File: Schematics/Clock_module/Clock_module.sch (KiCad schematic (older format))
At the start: 38 parts, among them J1 Conn_01x06_Female, J2 Power Input, SW1 Mode, SW2 Step, U1 NE555, U2 NE555, U3 NE555, U4 74LS04, U5 74LS32, U6 74LS08

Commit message: Redesign in progress
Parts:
- J2: symbol Connector:Barrel_Jack_MountingPin -> Connector:Barrel_Jack
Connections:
- no-connect marks 2 -> 1
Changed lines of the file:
@@
 	7900 5150 7900 5050
 $Comp
-L Connector:Barrel_Jack_MountingPin J2
+L Connector:Barrel_Jack J2
 U 1 1 5E4C3442
 P 2700 1400
@@
 	1    0    0    -1
 $EndComp
-NoConn ~ 2700 1700
 Wire Wire Line
 	3000 1300 3000 1250

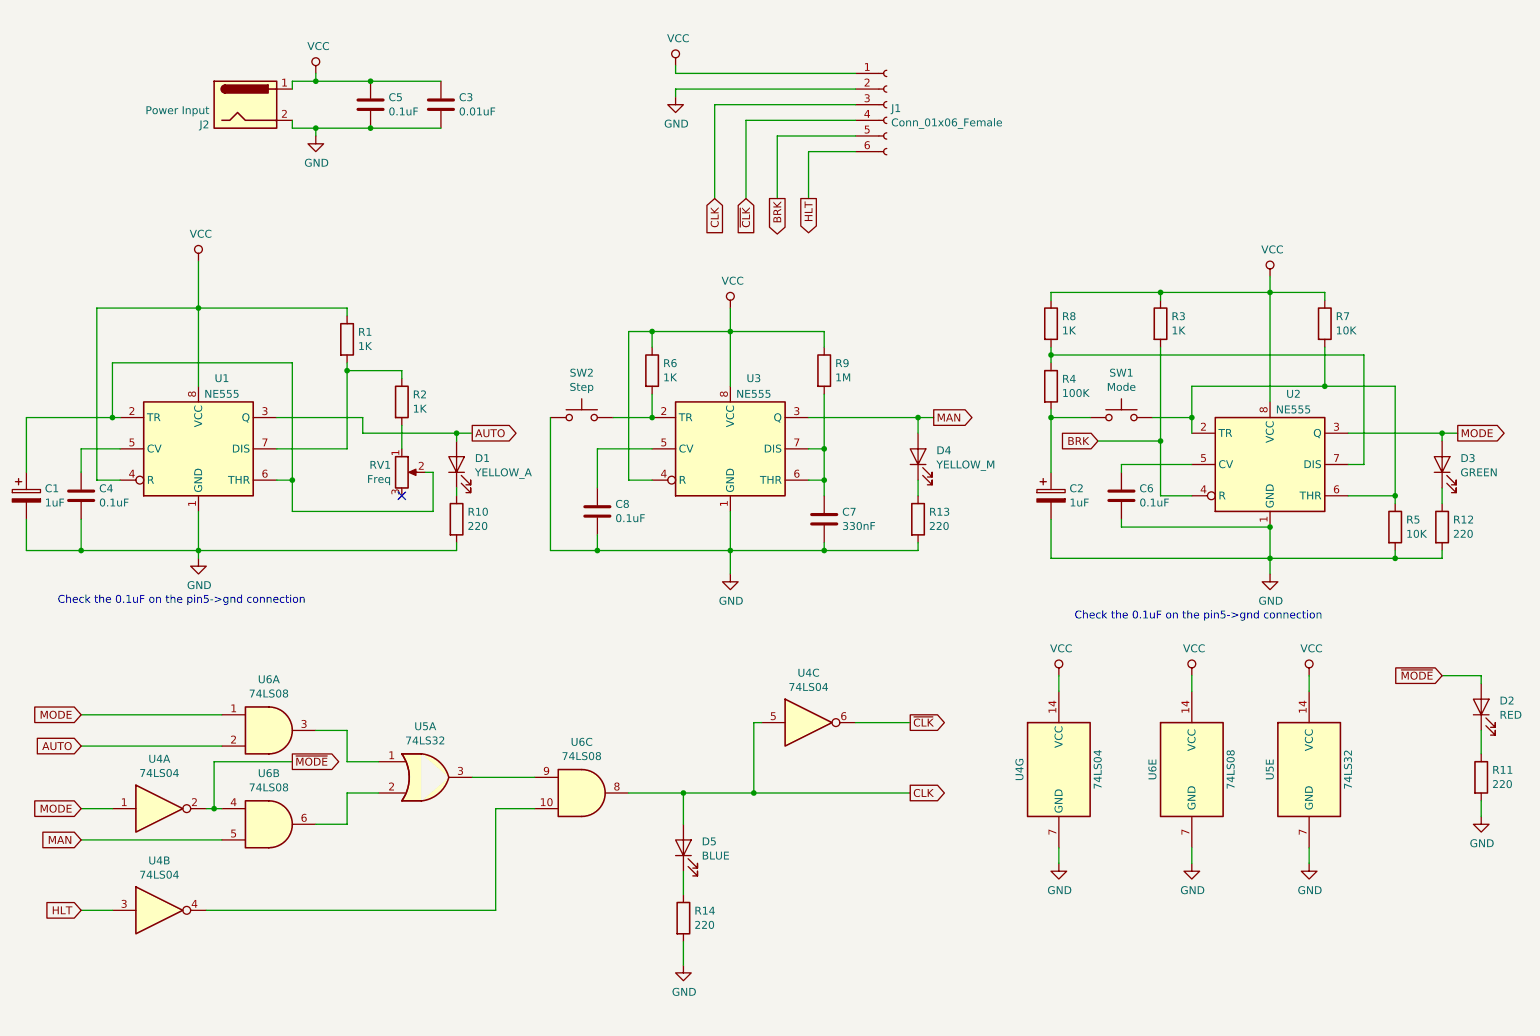
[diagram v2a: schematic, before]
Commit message: Added missing pull-down resistor to clock module
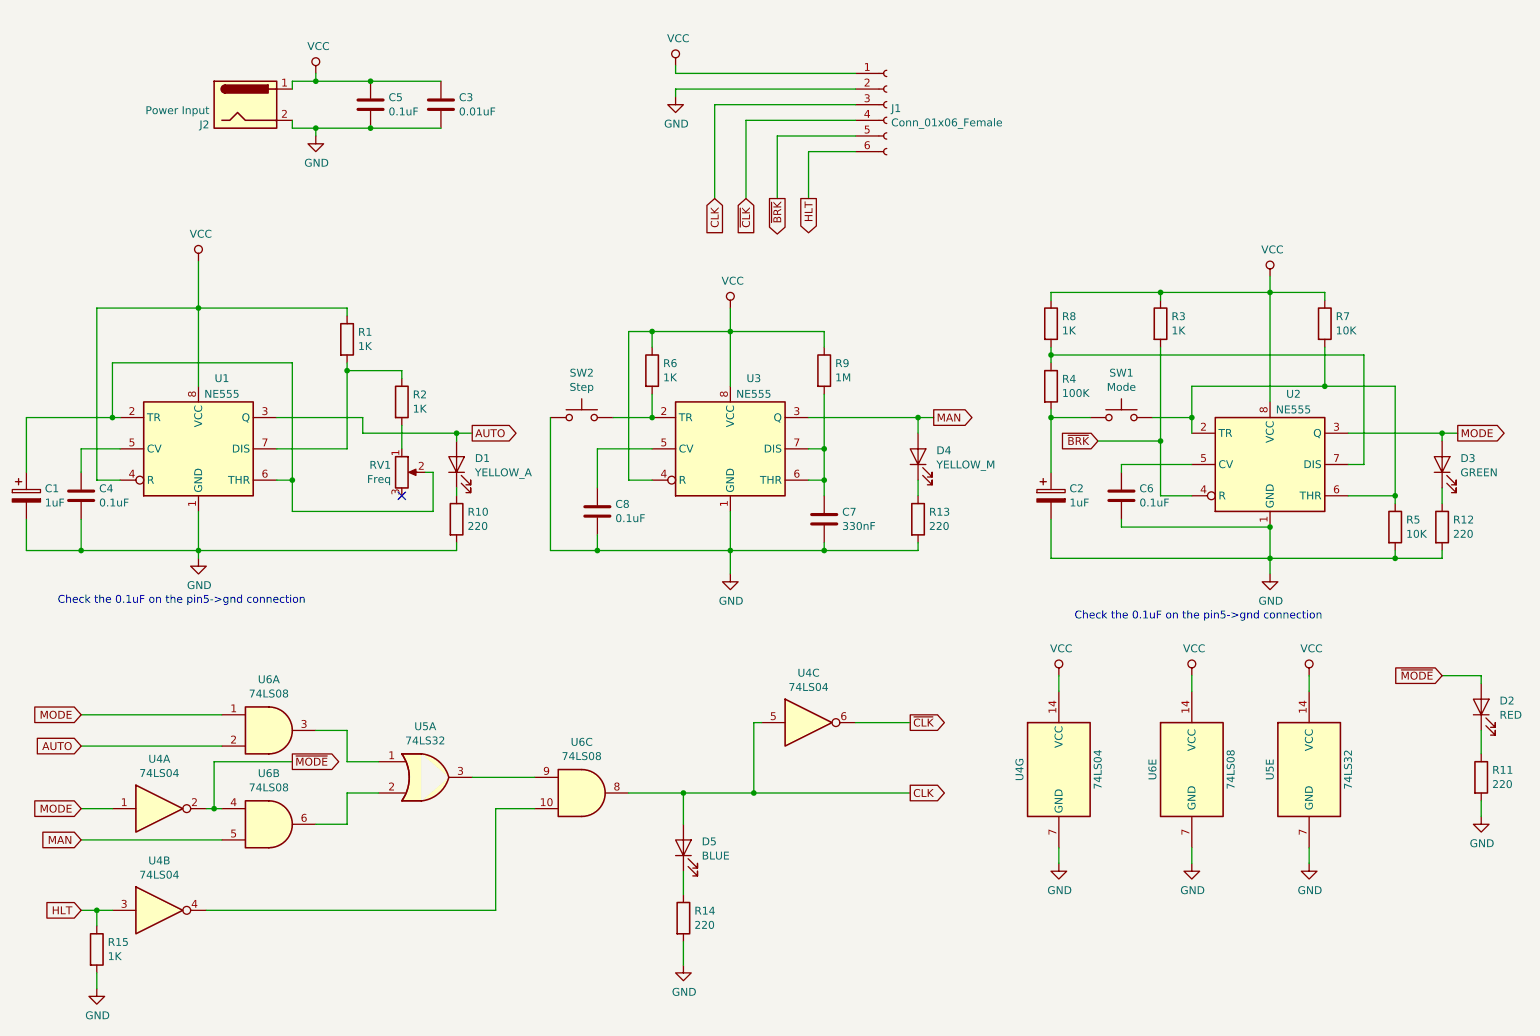
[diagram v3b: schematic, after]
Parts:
- added R15: 1K, Resistor_THT:R_Axial_DIN0207_L6.3mm_D2.5mm_P7.62mm_Horizontal, symbol Device:R
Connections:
- net GND: now also R15.2
- net HLT: now also R15.1
- net BRK renamed ~BRK
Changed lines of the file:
@@
 HLT
 Wire Wire Line
-	1650 6550 1850 6550
+	1650 6550 1750 6550
 $Comp
 L Device:R R11
@@
 	5900 1500 6600 1500
 Text GLabel 8150 3550 0    50   Input ~ 0
-BRK
+~BRK
 Wire Wire Line
 	8150 3550 8550 3550
@@
 	8550 3550 8550 2950
 Text GLabel 6100 2000 3    50   Output ~ 0
-BRK
+~BRK
 Wire Wire Line
 	6100 2000 6100 1600
@@
 Wire Wire Line
 	2400 2400 2400 2700
+$Comp
+L Device:R R15
+U 1 1 5E537F1F
+P 1750 6800
+F 0 "R15" H 1820 6846 50  0000 L CNN
+F 1 "1K" H 1820 6755 50  0000 L CNN
+F 2 "Resistor_THT:R_Axial_DIN0207_L6.3mm_D2.5mm_P7.62mm_Horizontal" V 1680 6800 50  0001 C CNN
+F 3 "~" H 1750 6800 50  0001 C CNN
+F 4 "100K" H 1750 6800 50  0001 C CNN "Value"
+	1    1750 6800
+	1    0    0    -1
+$EndComp
+Wire Wire Line
+	1750 6550 1750 6650
+Connection ~ 1750 6550
+Wire Wire Line
+	1750 6550 1850 6550
+$Comp
+L power:GND #PWR019
+U 1 1 5E54227B
+P 1750 7050
+F 0 "#PWR019" H 1750 6800 50  0001 C CNN
+F 1 "GND" H 1755 6877 50  0000 C CNN
+F 2 "" H 1750 7050 50  0001 C CNN
+F 3 "" H 1750 7050 50  0001 C CNN
+	1    1750 7050
+	1    0    0    -1
+$EndComp
+Wire Wire Line
+	1750 7050 1750 6950
 $EndSCHEMATC

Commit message: PCB RC6
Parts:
- added C9: 1uF, Capacitor_THT:CP_Radial_D5.0mm_P2.50mm, symbol Device:CP
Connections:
- net ~BRK: now also C9.2; no longer R3.2, U2.4 (R)
- new net: C9.1, R3.2, U2.4 (R)
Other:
- moved on the sheet: J2
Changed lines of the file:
@@
 L power:VCC #PWR01
 U 1 1 5DFD8BA7
-P 3150 1200
-F 0 "#PWR01" H 3150 1050 50  0001 C CNN
-F 1 "VCC" H 3167 1373 50  0000 C CNN
-F 2 "" H 3150 1200 50  0001 C CNN
-F 3 "" H 3150 1200 50  0001 C CNN
-	1    3150 1200
+P 3300 1200
+F 0 "#PWR01" H 3300 1050 50  0001 C CNN
+F 1 "VCC" H 3317 1373 50  0000 C CNN
+F 2 "" H 3300 1200 50  0001 C CNN
+F 3 "" H 3300 1200 50  0001 C CNN
+	1    3300 1200
 	1    0    0    -1
 $EndComp
@@
 L power:GND #PWR02
 U 1 1 5DFD94A3
-P 3150 1600
-F 0 "#PWR02" H 3150 1350 50  0001 C CNN
-F 1 "GND" H 3155 1427 50  0000 C CNN
-F 2 "" H 3150 1600 50  0001 C CNN
-F 3 "" H 3150 1600 50  0001 C CNN
-	1    3150 1600
+P 3300 1600
+F 0 "#PWR02" H 3300 1350 50  0001 C CNN
+F 1 "GND" H 3305 1427 50  0000 C CNN
+F 2 "" H 3300 1600 50  0001 C CNN
+F 3 "" H 3300 1600 50  0001 C CNN
+	1    3300 1600
 	1    0    0    -1
 $EndComp
@@
 Wire Wire Line
 	5900 1500 6600 1500
-Text GLabel 8150 3550 0    50   Input ~ 0
+Text GLabel 7750 3550 0    50   Input ~ 0
 ~BRK
-Wire Wire Line
-	8150 3550 8550 3550
 Connection ~ 8550 3550
 Wire Wire Line
@@
 L Connector:Barrel_Jack J2
 U 1 1 5E4C3442
-P 2700 1400
-F 0 "J2" H 2470 1272 50  0000 R CNN
-F 1 "Power Input" H 2470 1363 50  0000 R CNN
-F 2 "Connector_BarrelJack:BarrelJack_Horizontal" H 2750 1360 50  0001 C CNN
-F 3 "~" H 2750 1360 50  0001 C CNN
-	1    2700 1400
-	1    0    0    -1
-$EndComp
-Wire Wire Line
-	3000 1300 3000 1250
-Wire Wire Line
-	3000 1250 3150 1250
-Wire Wire Line
-	3000 1500 3000 1550
-Wire Wire Line
-	3000 1550 3150 1550
-Wire Wire Line
-	3150 1550 3150 1600
-Connection ~ 3150 1550
-Wire Wire Line
-	3150 1550 3500 1550
-Wire Wire Line
-	3150 1200 3150 1250
-Connection ~ 3150 1250
-Wire Wire Line
-	3150 1250 3500 1250
+P 2350 1400
+F 0 "J2" H 2120 1272 50  0000 R CNN
+F 1 "Power Input" H 2120 1363 50  0000 R CNN
+F 2 "Connector_BarrelJack:BarrelJack_Horizontal" H 2400 1360 50  0001 C CNN
+F 3 "~" H 2400 1360 50  0001 C CNN
+	1    2350 1400
+	1    0    0    -1
+$EndComp
+Wire Wire Line
+	3300 1550 3300 1600
+Wire Wire Line
+	3300 1550 3500 1550
+Wire Wire Line
+	3300 1200 3300 1250
+Wire Wire Line
+	3300 1250 3500 1250
 Wire Wire Line
 	2400 2400 2400 2700
@@
 Wire Wire Line
 	1750 7050 1750 6950
+$Comp
+L Device:CP C9
+U 1 1 5E533099
+P 8150 3550
+F 0 "C9" V 8300 3550 50  0000 L CNN
+F 1 "1uF" V 8300 3400 50  0000 L CNN
+F 2 "Capacitor_THT:CP_Radial_D5.0mm_P2.50mm" H 8188 3400 50  0001 C CNN
+F 3 "~" H 8150 3550 50  0001 C CNN
+F 4 "1uF" H 8150 3550 50  0001 C CNN "Value"
+	1    8150 3550
+	0    1    1    0
+$EndComp
+Wire Wire Line
+	8300 3550 8550 3550
+Wire Wire Line
+	7750 3550 8000 3550
+$Comp
+L power:PWR_FLAG #FLG01
+U 1 1 5E58F759
+P 2950 1200
+F 0 "#FLG01" H 2950 1275 50  0001 C CNN
+F 1 "PWR_FLAG" H 2950 1373 50  0000 C CNN
+F 2 "" H 2950 1200 50  0001 C CNN
+F 3 "~" H 2950 1200 50  0001 C CNN
+	1    2950 1200
+	1    0    0    -1
+$EndComp
+Wire Wire Line
+	2950 1200 2950 1250
+Wire Wire Line
+	2950 1300 2650 1300
+Wire Wire Line
+	2650 1500 2950 1500
+Wire Wire Line
+	2950 1500 2950 1550
+Wire Wire Line
+	2950 1550 3300 1550
+Connection ~ 3300 1550
+Wire Wire Line
+	2950 1250 3300 1250
+Connection ~ 2950 1250
+Wire Wire Line
+	2950 1250 2950 1300
+Connection ~ 3300 1250
 $EndSCHEMATC

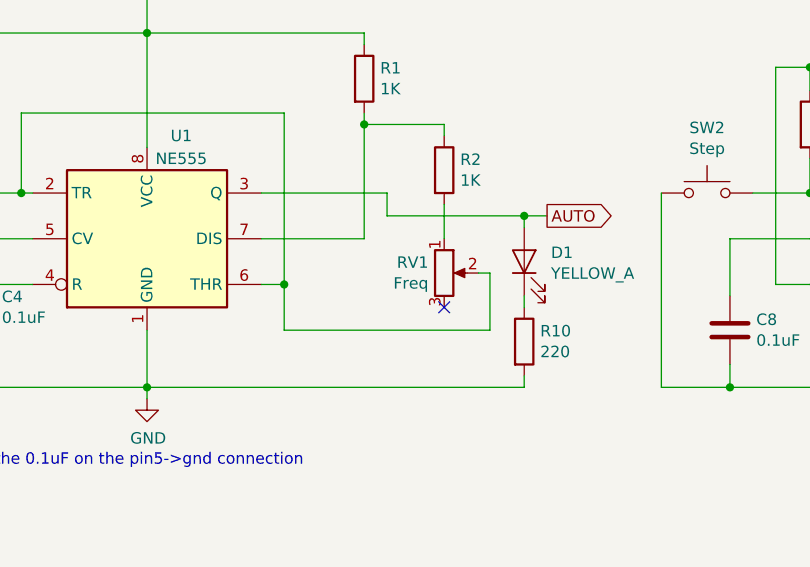
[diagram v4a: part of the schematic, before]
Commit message: PCB RC9 - replaced potentiometers
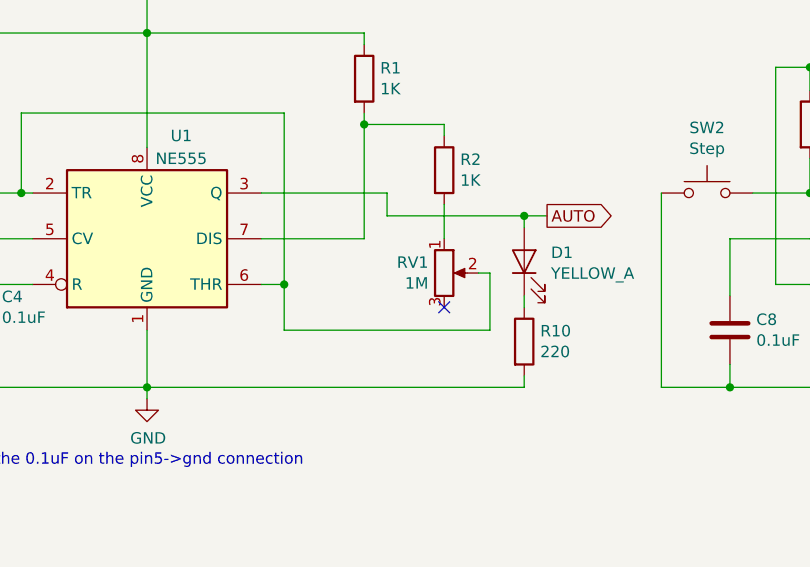
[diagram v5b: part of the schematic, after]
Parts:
- RV1: value Freq -> 1M; footprint Potentiometer_THT:Potentiometer_Runtron_RM-065_Vertical -> Potentiometer_THT:Potentiometer_Piher_PT-10-V10_Vertical
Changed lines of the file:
@@
 P 3700 3750
 F 0 "RV1" H 3631 3796 50  0000 R CNN
-F 1 "Freq" H 3631 3705 50  0000 R CNN
-F 2 "Potentiometer_THT:Potentiometer_Runtron_RM-065_Vertical" H 3700 3750 50  0001 C CNN
+F 1 "1M" H 3631 3705 50  0000 R CNN
+F 2 "Potentiometer_THT:Potentiometer_Piher_PT-10-V10_Vertical" H 3700 3750 50  0001 C CNN
 F 3 "~" H 3700 3750 50  0001 C CNN
 	1    3700 3750

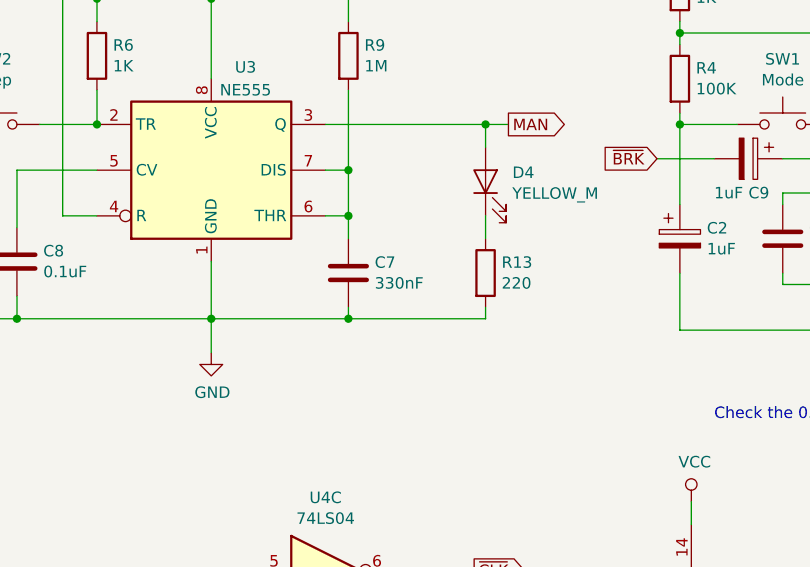
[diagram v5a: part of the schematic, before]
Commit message: Updated schematic to match changes to BOM
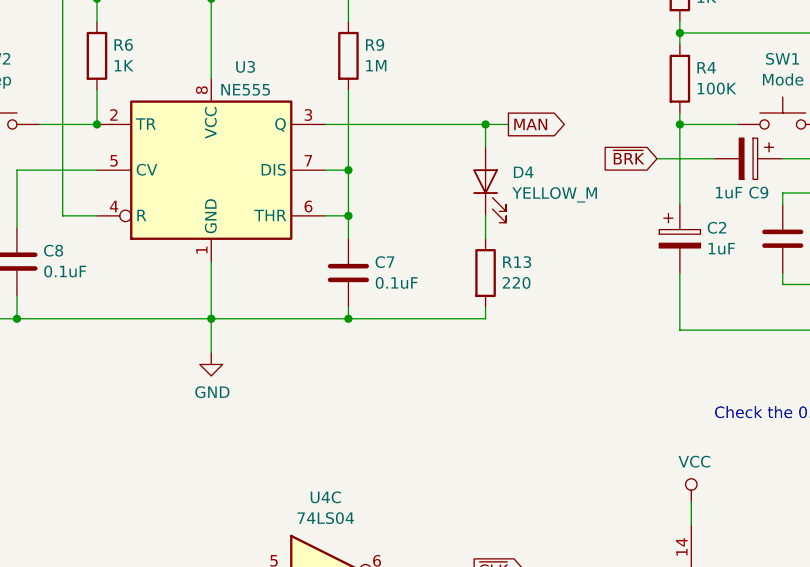
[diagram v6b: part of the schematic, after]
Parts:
- C7: value 330nF -> 0.1uF
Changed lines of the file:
@@
 P 6400 4050
 F 0 "C7" H 6515 4096 50  0000 L CNN
-F 1 "330nF" H 6515 4005 50  0000 L CNN
+F 1 "0.1uF" H 6515 4005 50  0000 L CNN
 F 2 "Capacitor_THT:C_Disc_D3.0mm_W2.0mm_P2.50mm" H 6438 3900 50  0001 C CNN
 F 3 "~" H 6400 4050 50  0001 C CNN
